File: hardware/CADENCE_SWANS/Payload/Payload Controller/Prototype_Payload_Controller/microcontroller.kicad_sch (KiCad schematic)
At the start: 3 parts, among them U8 ATSAMV71Q21B-A

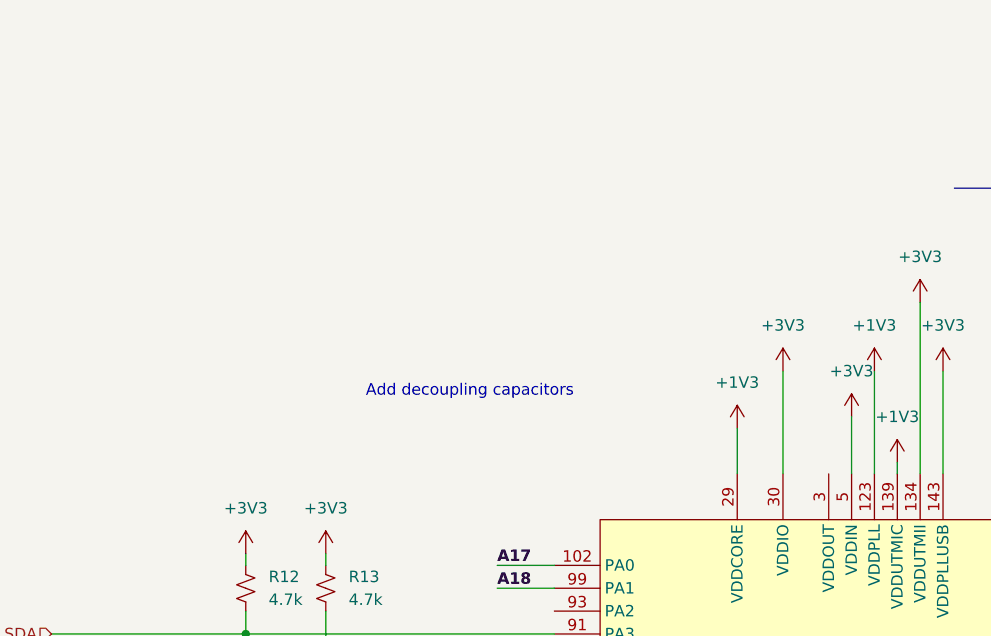
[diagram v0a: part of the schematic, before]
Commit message: in the process of adding decoupling capacitors
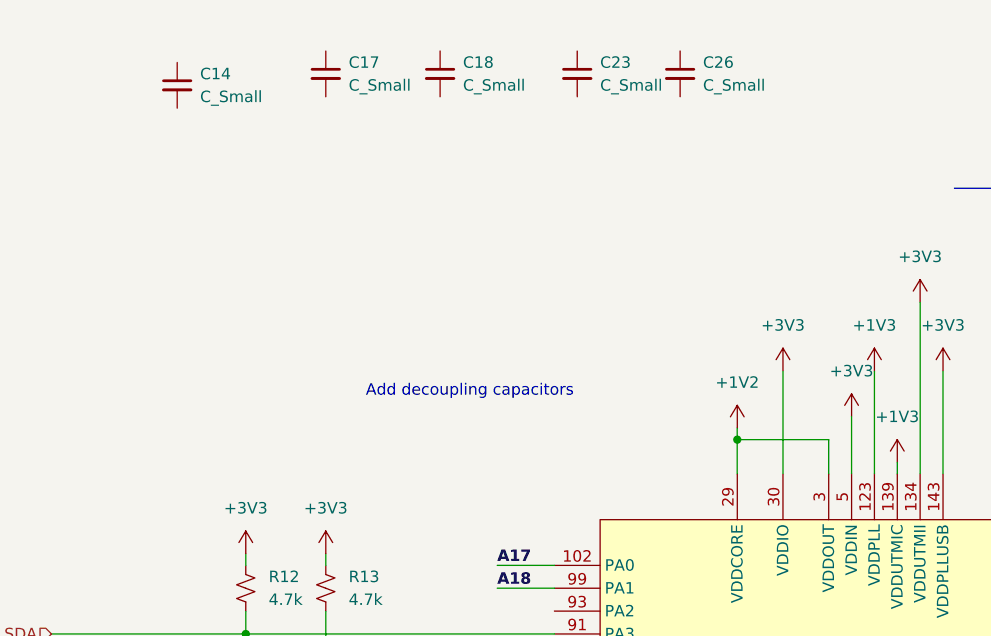
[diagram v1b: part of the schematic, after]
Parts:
- added C14, C17, C18, C23, C26: C_Small, symbol Device:C_Small
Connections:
- net +1V3: no longer U8.107 (VDDCORE), U8.29 (VDDCORE), U8.33 (VDDCORE), U8.50 (VDDCORE), U8.81 (VDDCORE)
- net +1V2: now reaches U8.3 (VDDOUT)
- net +1V2: now also U8.107 (VDDCORE), U8.29 (VDDCORE), U8.33 (VDDCORE), U8.50 (VDDCORE), U8.81 (VDDCORE)

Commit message: added decoupling capacitors
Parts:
- added C27, C28, C29, C30, C31, C32, C33, C34, C35, C37: 100nF, symbol Device:C_Small
- added C38: 4.7uF, symbol Device:C_Small
- C14, C17, C18, C23, C26: value C_Small -> 100nF
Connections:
- net +1V3 is gone; now on net +1V2: U8.123 (VDDPLL), U8.139 (VDDUTMIC)
- net +1V2: now also C27.1, C28.1, C29.1, C30.1, C31.1, C35.1, C37.1
- net +3V3: now also C14.1, C17.1, C18.1, C23.1, C26.1, C32.1, C33.1, C34.1, C38.1
- net GND: now also C14.2, C17.2, C18.2, C23.2, C26.2, C27.2, C28.2, C29.2, C30.2, C31.2, C32.2, C33.2, C34.2, C35.2, C37.2, C38.2
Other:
- note added: "VDDCORE Decoupling Capacitors"
- note added: "VDDIN Decoupling Capacitors"
- note added: "VDDIO Decoupling Capacitors"
- note added: "VDDOUT Decoupling Capacitors"
- note added: "VDDPLL Decoupling Capacitors"
- note added: "VDDPLLUSB Decoupling Capacitors"
- note added: "VDDUTMIC Decoupling Capacitors"
- note added: "VDDUTMII Decoupling Capacitors"
- note removed: "Add decoupling capacitors"
- note removed: "Configure Real Time Clock (RTC)"
- moved on the sheet: C14, R12, R13, U8

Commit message: identified debug and usb pins
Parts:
- C32: value 100nF -> 4.7uF
- C38: value 4.7uF -> 1uF
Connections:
- net GND: now also U8.85 (TST)
- net Payload_Rx: now also U8.52 (PD25); no longer U8.66 (PA10)
- net Payload_Tx: now also U8.53 (PD26); no longer U8.75 (PA9)
- net USB_D-: now reaches U8.136 (HSDM)
- net USB_D+: now reaches U8.137 (HSDP)
- net XOUT: now reaches U8.141 (PB8)
- net XIN: now reaches U8.142 (PB9)
- net XIN32: now reaches U8.35 (PA7)
- net XOUT32: now reaches U8.36 (PA8)
- net SWDIO: now reaches U8.79 (PB6)
- net NRST: now reaches U8.83 (NRST)
- net ERASE: now reaches U8.87 (PB12)
- net SWCLK: now reaches U8.89 (PB7)
- new net URXD0: U8.75 (PA9)
- new net UTXD0: U8.66 (PA10)
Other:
- note added: "BOOT"
- note added: "Debug Section"
- note added: "Note: Place close to power supply pins"
- note added: "Serial Wire Debug (SWD)"
- note added: "USB"
- note added: "VDDOUT will supply VDDCORE, VDDPLL and VDDUTMIC"

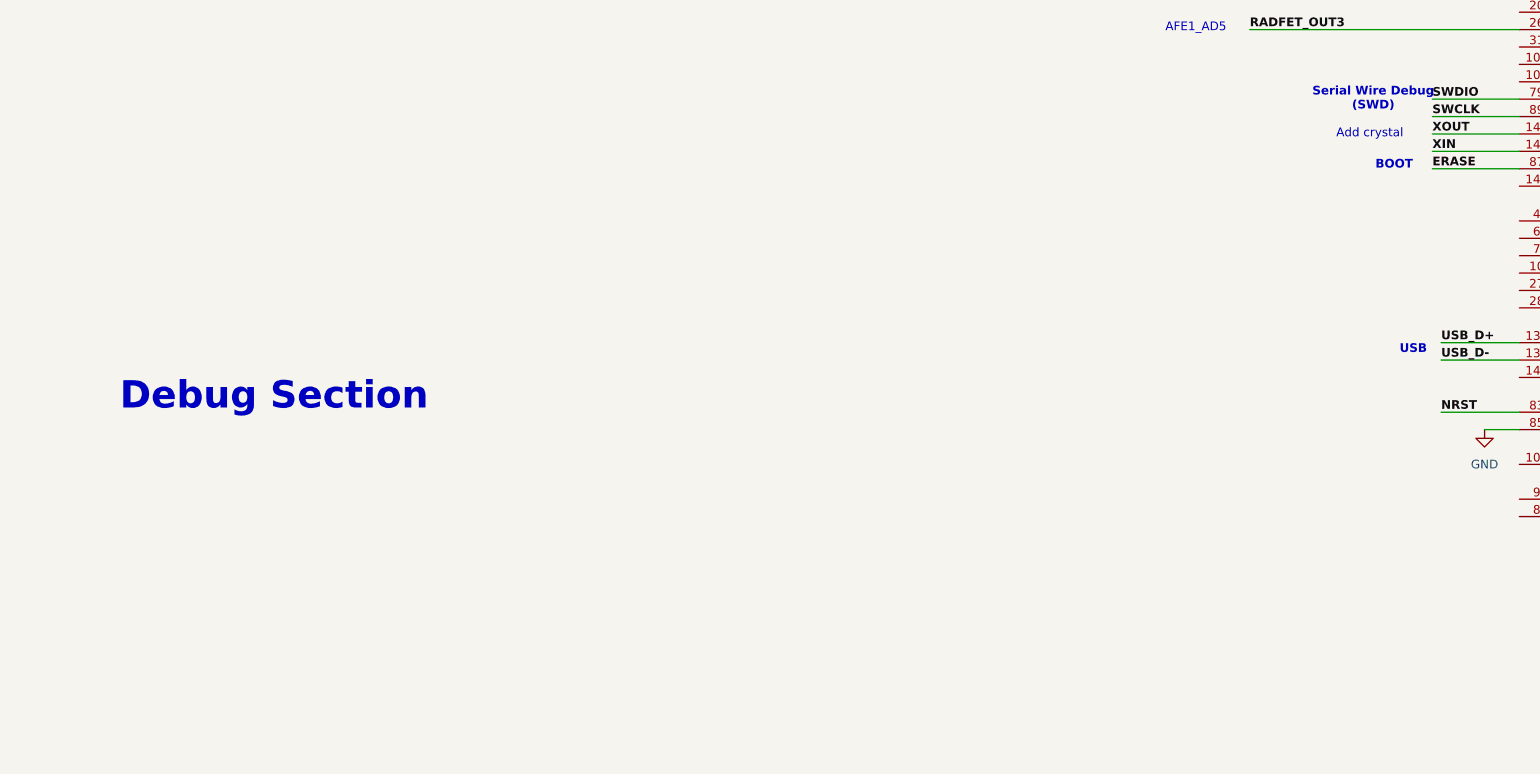
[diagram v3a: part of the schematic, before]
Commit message: implemented usb-c and broke out debug ports
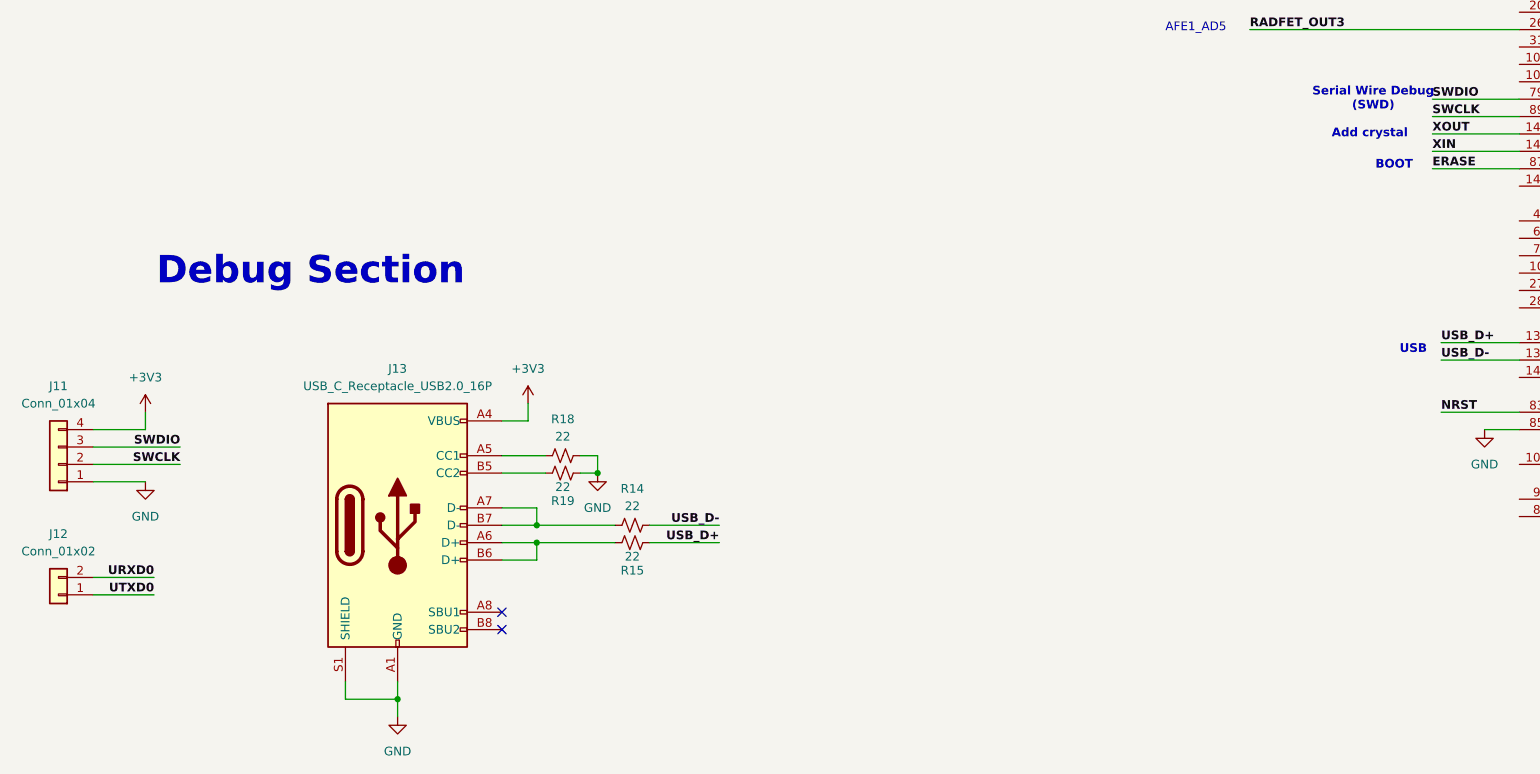
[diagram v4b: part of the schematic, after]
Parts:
- added J11: Conn_01x04, symbol Connector_Generic:Conn_01x04
- added J12: Conn_01x02, symbol Connector_Generic:Conn_01x02
- added J13: USB_C_Receptacle_USB2.0_16P, symbol Connector:USB_C_Receptacle_USB2.0_16P
- added R14, R15, R18, R19: 22, symbol Device:R_Small_US
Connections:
- net +3V3: now also J11.4 (Pin_4), J13.A4 (VBUS), J13.A9 (VBUS), J13.B4 (VBUS), J13.B9 (VBUS)
- net GND: now also J11.1 (Pin_1), J13.A1 (GND), J13.A12 (GND), J13.B1 (GND), J13.B12 (GND), J13.S1 (SHIELD), R18.1, R19.2
- net SWCLK: now also J11.2 (Pin_2)
- net SWDIO: now also J11.3 (Pin_3)
- net URXD0: now also J12.2 (Pin_2)
- net USB_D+: now also R15.2
- net USB_D-: now also R14.1
- net UTXD0: now also J12.1 (Pin_1)
- new net: J13.A5 (CC1), R18.2
- new net: J13.A6 (D+), J13.B6 (D+), R15.1
- new net: J13.A7 (D-), J13.B7 (D-), R14.2
- new net: J13.B5 (CC2), R19.1
- no-connect marks 0 -> 2

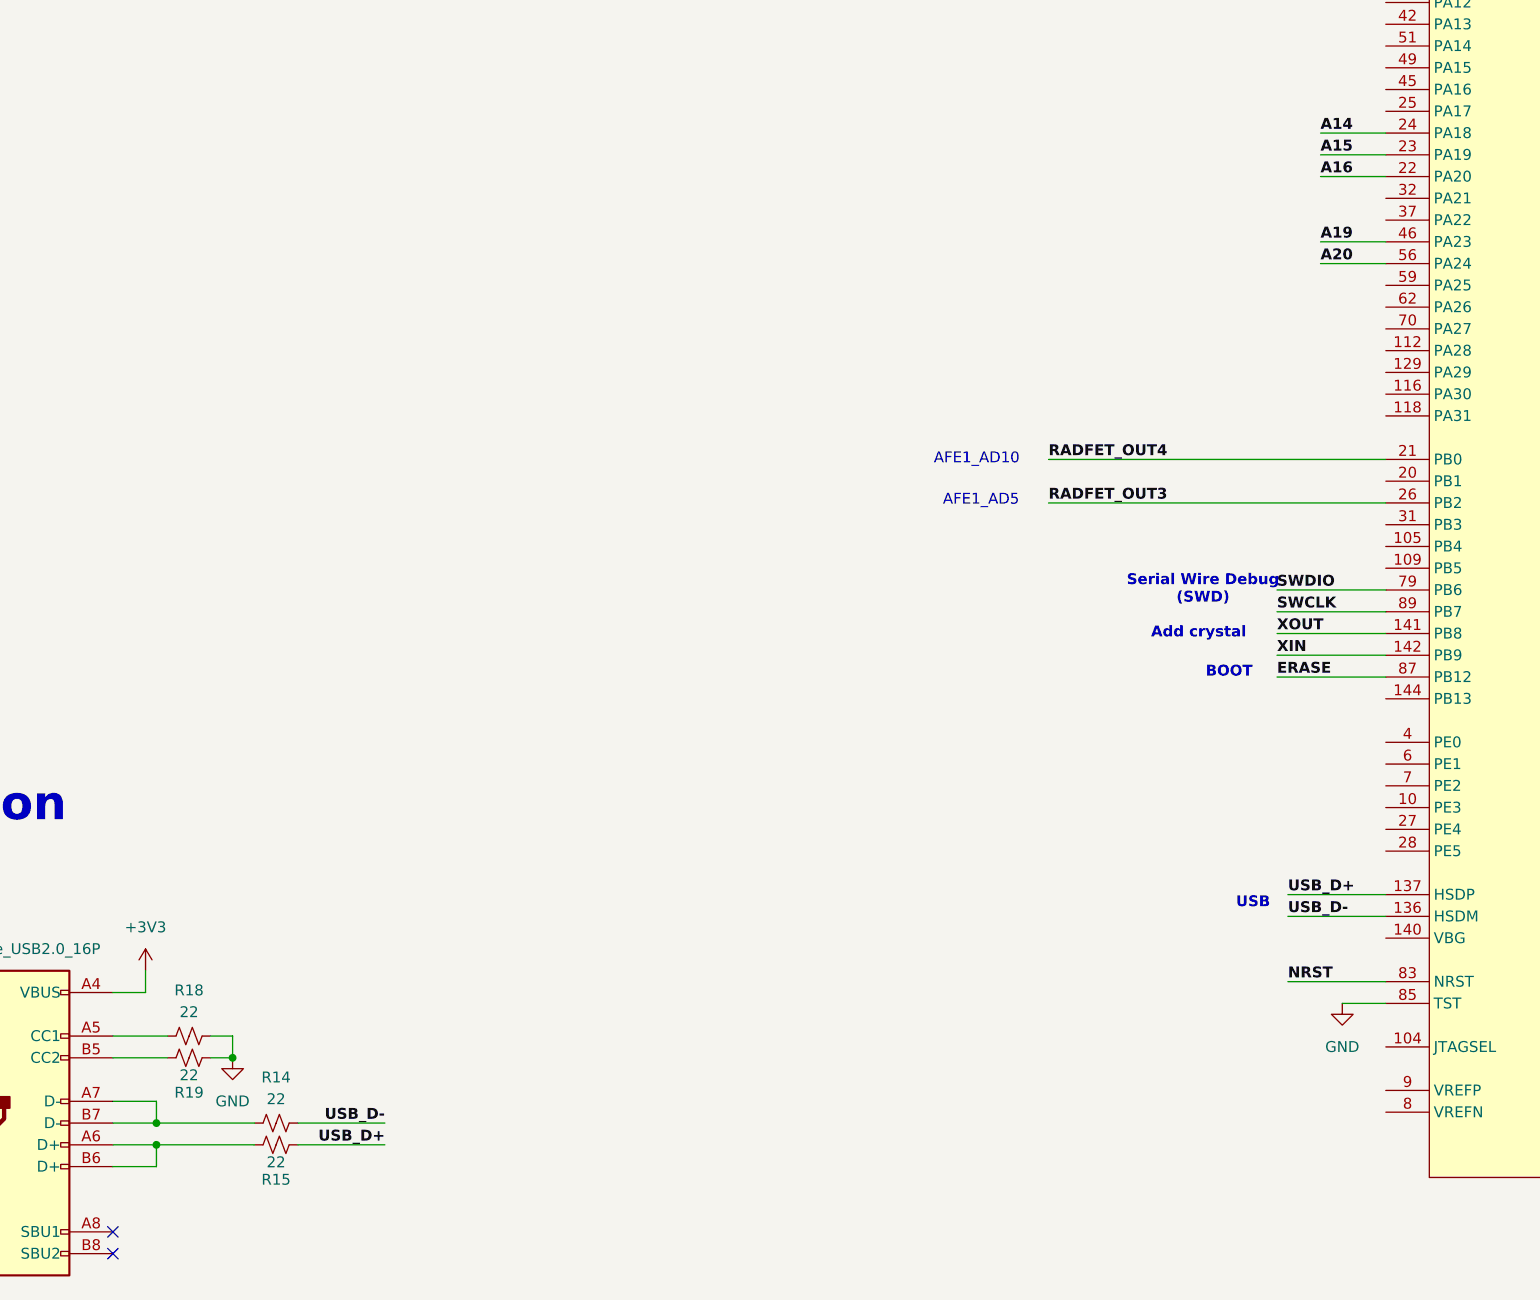
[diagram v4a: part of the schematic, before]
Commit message: implemented erase and reset buttons
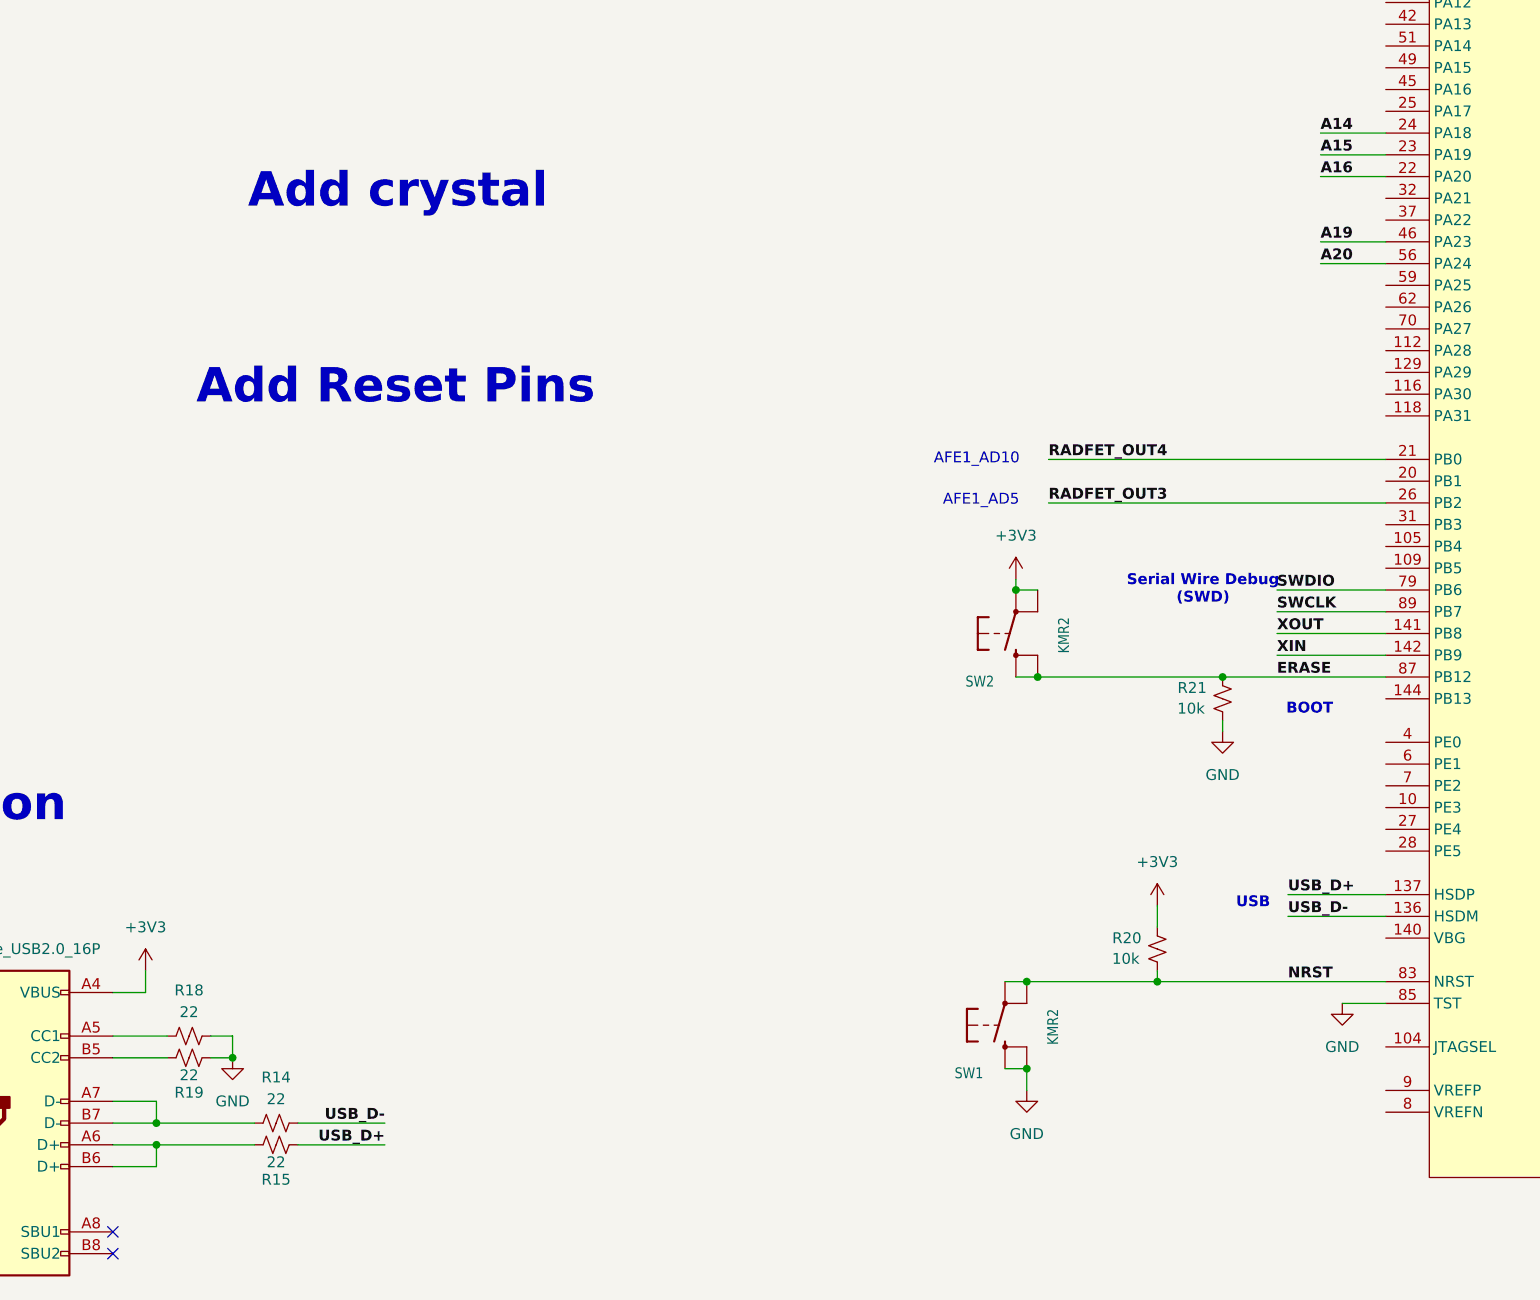
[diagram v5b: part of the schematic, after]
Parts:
- added R20, R21: 10k, symbol Device:R_Small_US
- added SW1, SW2: KMR2, FC_DEV_BOARD:BTN_KMR2_4.6X2.8, symbol Adafruit ItsyBitsy RP2040-eagle-import:SWITCH_TACT_SMT4.6X2.8
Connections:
- net +3V3: now also R20.1, SW2.A (P), SW2.A' (P1)
- net ERASE: now also R21.1, SW2.B (S), SW2.B' (S1)
- net GND: now also R21.2, SW1.B (S), SW1.B' (S1)
- net NRST: now also R20.2, SW1.A (P), SW1.A' (P1)
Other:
- note added: "Add Reset Pins"

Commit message: changed CC1 and CC2 resistor values
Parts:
- R18, R19: value 22 -> 5.1k
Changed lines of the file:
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@@
 			)
 		)
-		(property "Value" "22"
+		(property "Value" "5.1k"
 			(at 119.38 326.136 90)
 			(effects
@@
 			)
 		)
-		(property "Value" "22"
+		(property "Value" "5.1k"
 			(at 119.38 333.502 90)
 			(effects
